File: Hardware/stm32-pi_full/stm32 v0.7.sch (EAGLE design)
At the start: 199 parts, among them Q1 MMBT3906, Q2 MMBT3904, Q3 MMBT3904, U1 ESP32-WROOM-32D

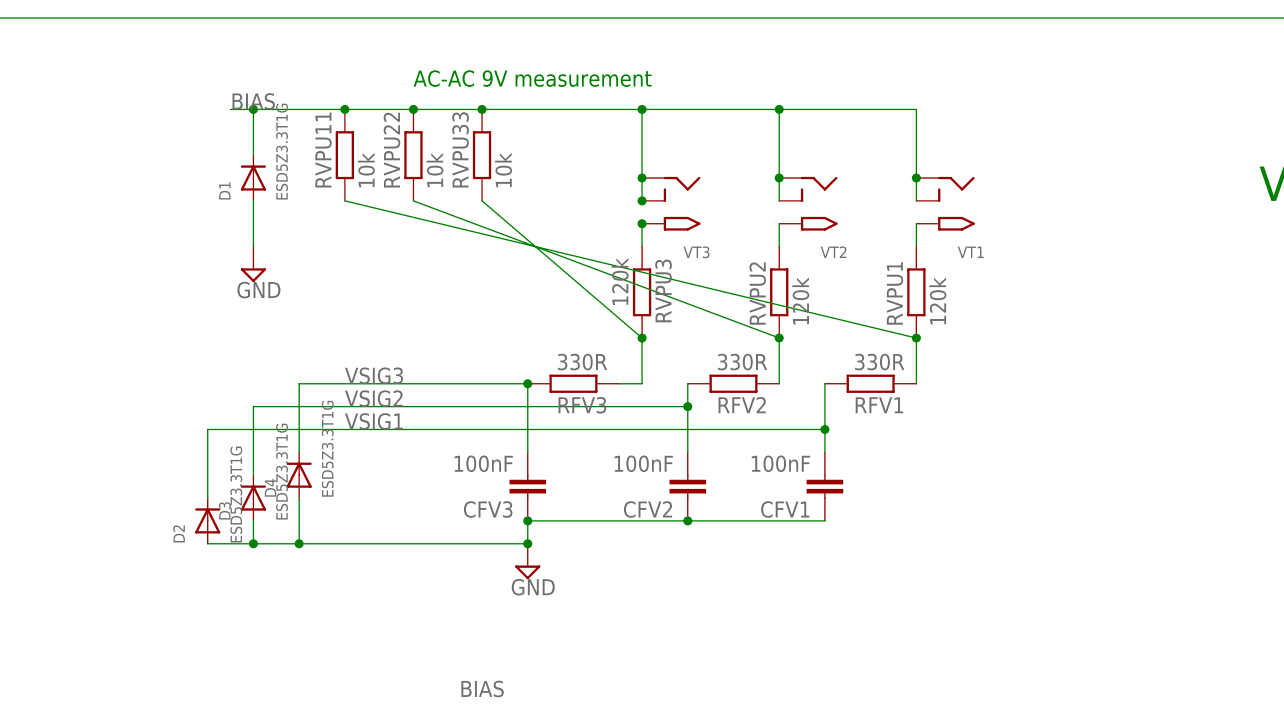
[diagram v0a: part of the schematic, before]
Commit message: commit JSON parser and arm_math examples
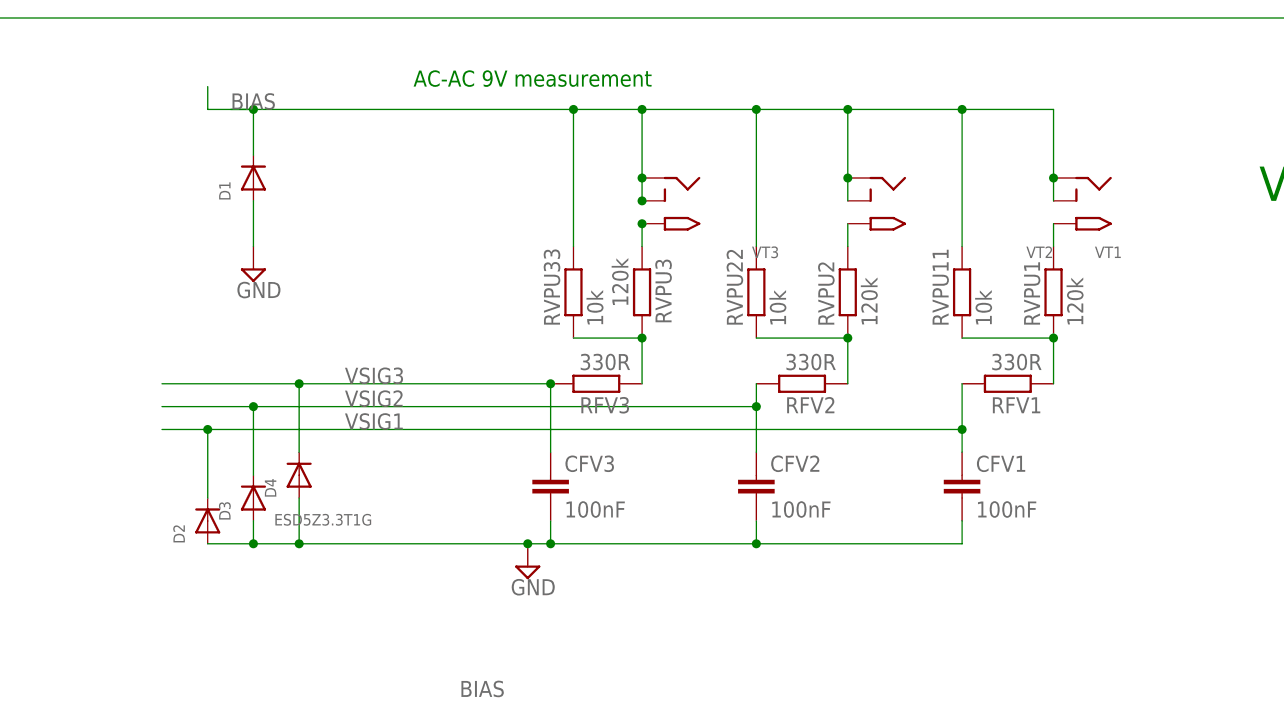
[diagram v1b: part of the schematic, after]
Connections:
- net GND: now also CFV1.2, CFV2.2, CFV3.2; no longer CFV1.1, CFV2.1, CFV3.1
- net VSIG1: now also CFV1.1; no longer CFV1.2
- net VSIG2: now also CFV2.1; no longer CFV2.2
- net VSIG3: now also CFV3.1; no longer CFV3.2
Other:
- moved on the sheet: CFV1, CFV2, CFV3, RFV1, RFV2, RFV3, RVPU1, RVPU11, RVPU2, RVPU22, RVPU33, VT1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

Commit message: update, plus reports
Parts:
- removed 3POLE_1, 3POLE_2, 3POLE_3, 3POLE_6, 3POLE_7: OMNIMATE_LSF_3COMBICON_SMT_3, OMNIMATE_LSF:OMNIMATE_LSF_3COMBICON_SMT_3
- removed C15, C21: 100nF, resistor:C-EUC0603
- removed C23: (no value), rcl:CPOL-EU153CLV-1010
- removed D14, D15, D16, D19: ESD5Z3.3T1G, microbuilder:DIODESOD-523
- removed D20: (no value), diode:SUPPRESSOR-SMBJ
- removed JP3: (no value), pinhead+:PINHD-1X81X08_SMT
- added BIAS_IN, ST_LINK: (no value), SparkFun:M02PTH
- added C1, C19, C20, C22: 100nF, resistor:C-EUC0603
- added D17, D18, D21, D26, D40*1: ESD5Z3.3T1G, microbuilder:DIODESOD-523
- added G1: CH291-1220LF, CH291-1220LF:CH291-1220LF
- added J1, SJ23, SJ24, SJ25, SJ26, SJ27, SJ28, SJ29, SJ30, SJ32: SOLDERJUMPERNO, SparkFun:SOLDERJUMPERNO
- added OLED: (no value), con-lstb-db:MA04-1-OLEDOLED
- added R7: 4.7k, resistor:R-EU_R0603
- added R8: 1k, resistor:R-EU_R0603
- added UART_2: (no value), pinhead+:PINHD-1X61X06_SMT
- C10: value 100nF -> 2.2uF; device resistor:C-EUC0603 -> rcl:C-EUC0805
- C11: value 10nF -> 2.2uF; device rcl:C-EUC0603 -> rcl:C-EUC0805
- C12, C7: value 1uF -> 4.7uF
- C13: value 10nF -> 100nF
- C14, C17: value 1uF -> 2.2uF
- C24, C25, C3, C4: value 4.7uF -> 2.2uF
- C50*: value 1uF -> 2.2uF; device rcl:C-EUC0603 -> rcl:C-EUC0805
- SJ22: value (none) -> SOLDERJUMPERNO; device jumper-con_db:SJ-CONCON -> SparkFun:SOLDERJUMPERNO
- renumbered JP1 to UART_ESP
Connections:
- net N$11 renamed RXD0_ESP
- net N$16 renamed CS_STM32_RPI
- net N$7 renamed TXD0_ESP
- removed net +3V3_ADC: C11.1, C12.1, C7.1, SJ2.2, STM32F303VE.VREF+, VREF_3V3.OUT
- removed net N$21: R6.1, SJ22.2
- removed net N$23: STM32F303VE.PA10, UART1.1
- new net +3V3_ESP: SJ23.1, U1.3V3
- new net BOOT0_RPI: J1.2, PCB2.GPIO4
- new net N$16: Q4.S, R8.1
- new net NRST_STM_ESP: SJ25.1, U1.IO18
- new net NRST_STM_RPI: PCB2.GPIO17, SJ32.2
- new net RPI_GPIO16_RPI: PCB2.GPIO16, SJ29.1
- new net RPI_GPIO20_RPI: PCB2.GPIO20, SJ30.1
- new net RST_RFM_ESP: SJ24.1, U1.IO17
- new net RST_RFM_RPI: PCB2.GPIO5, SJ28.2
- new net SCL_RPI: PCB2.ID_SC*, SJ27.1
- new net SDA_RPI: PCB2.ID_SD*, SJ26.2
- new net VDD_MCP1501: C11.1, SJ22.2, VREF_3V3.SHT_DN, VREF_3V3.VDD
- new net VREF+: SJ2.2, STM32F303VE.VREF+, VREF_3V3.OUT
- net +3V3: now also BIAS_IN.1, OLED.3, R6.1, R7.2, SJ23.2, U$1.P$1, U$3.P$1, U$4.P$1, U$5.P$1; no longer 3POLE_1.1, 3POLE_2.1, 3POLE_3.1, 3POLE_6.1, R22.2, SJ22.1, U1.3V3, UART_ESP.2, VREF_3V3.SHT_DN
- net +5V: now also C10.1, C12.2, C7.1, D40*1.C, SJ22.1, UART_2.3; no longer D20.C, JP3.3, VREF_3V3.VDD
- net 24V: now also U$6.P$1; no longer 3POLE_7.3
- net BOOT0: now also J1.1
- net BUTTON1: now also PCB2.GPIO27; no longer PCB2.GPIO4
- net DS18B20_2_RJ45: now also R7.1, STM32F303VE.PD0
- net GND: now also C1.2, C12.1, C19.2, C20.2, C22.2, D17.A, D18.A, D21.A, D26.A, D40*1.A, G1.-, OLED.4, U$1.P$3, U$3.P$3, U$4.P$3, U$5.P$3, U$6.P$3, UART_2.1; no longer 3POLE_1.3, 3POLE_2.3, 3POLE_3.3, 3POLE_6.3, 3POLE_7.1, C12.2, C15.2, C21.2, C23.-, D14.A, D15.A, D16.A, D19.A, D20.A, JP3.1
- net MBUS_INPUT: now also U$6.P$2; no longer 3POLE_7.2
- net N$1: now also UART_2.2; no longer JP3.2
- net N$12: now also BIAS_IN.2, R22.2; no longer STM32F303VE.PA9, UART1.2
- net NRST_STM: now also SJ25.2, SJ32.1, UART_2.6; no longer JP3.6, PCB2.GPIO6, U1.IO18
- net PUSHIN_1: now also C1.1, D17.C, U$1.P$2; no longer 3POLE_1.2, D14.C
- net PUSHIN_2: now also C19.1, D18.C, U$3.P$2; no longer 3POLE_2.2, C10.1, D15.C
- net PUSHIN_3: now also C20.1, D21.C, U$4.P$2; no longer 3POLE_3.2, C15.1, D16.C
- net PUSHIN_BYANT: now also C22.1, D26.C, U$5.P$2; no longer 3POLE_6.2, C21.1, D19.C
- net RPI_GPIO16: now also SJ29.2; no longer PCB2.GPIO16
- net RPI_GPIO20: now also SJ30.2; no longer PCB2.GPIO20
- net RST_RFM: now also SJ24.2, SJ28.1; no longer PCB2.GPIO5, U1.IO17
- net SCL: now also OLED.2, SJ27.2; no longer PCB2.ID_SC*
- net SDA: now also OLED.1, SJ26.1; no longer PCB2.ID_SD*
- net SWCLK: now also ST_LINK.1; no longer JP3.7
- net SWDIO: now also ST_LINK.2; no longer JP3.8
- net UART1_RX: now also STM32F303VE.PA10, UART1.1
- net UART1_TX: now also STM32F303VE.PA9, UART1.2
- net UART2_RX: now also UART_2.4; no longer JP3.4
- net UART2_TX: now also UART_2.5; no longer JP3.5
- net VBAT: now also G1.+, R8.2; no longer C23.+, Q4.S
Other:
- note added: "BATTERY_BACKUP"
- note added: "BIAS"
- note added: "Connectors"
- note added: "Expansion"
- note added: "LEDs"
- note added: "OLED"
- note added: "PUSH_BUTTON"
- note added: "USB"
- note added: "VTs and CTs"
- note removed: "Combined UART & ST-LINK Standard UART pin order SWDIO + SWCLK added to the top"
- note removed: "VT and CT inputs"
- moved on the sheet: BOOT_STM, C10, C11, C12, C18, C27, C28, C40, C41, C42, C45, C46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

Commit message: board v0.7
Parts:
- removed D24, D25, D40*, D41*: ESD5Z3.3T1G, microbuilder:DIODESOD-523
- removed SJ22: SOLDERJUMPERNO, SparkFun:SOLDERJUMPERNO
- removed UART_2, UART_ESP: (no value), pinhead+:PINHD-1X61X06_SMT
- added C15, C21, C31, C32: 2.2uF, rcl:C-EUC0805
- added C23: 200pF*, rcl:C-EUC0603
- added C29, C30: 5nF, rcl:C-EUC0603
- added JP1: JUMPER-SMT_3_1-NC_TRACE_NO-SILK, SparkFun-Jumpers:JUMPER-SMT_3_1-NC_TRACE_NO-SILK
- added R12: 330R, rcl:R-EU_R0603
- added R13, R20: 10k, resistor:R-EU_R0603
- added R21: 200k, resistor:R-EU_R0603
- added SJ31, SJ33: SOLDERJUMPERNO, SparkFun:SOLDERJUMPERNO
- added SV1, SV2: (no value), con-lstb-db:MA06-1
- C12, C18, C27, C7: value 4.7uF -> 2.2uF
- CT1, CT2, CT3, CT4, CT5, CT6, CT7, CT8, CT9: value STEREO_SMD -> SJ-3523-SMT; MPN (none) -> SJ-3523-SMT
- D40*1: value ESD5Z3.3T1G -> ESD5Z5.0T1G
- HSE: value 8MHZ ~15pFmax -> 406C35E08M00000
- PCB2: value RPI3YA -> TSM-120-01-T-DV
- R10, R3, R4, R5: value 220R -> 330R
- R18, R19: value 1K -> 1k
- R6: value 1.5K -> 1k
- R8: value 1k -> 1.5k
- RB1, RB2, RB3, RB4, RB5, RB6, RB7, RB8, RB9: device resistor:R-EU_R0603 -> rcl:R-EU_R1206
- STM32F303VE: value STM32F303XB -> STM32F303VE
- VT1, VT2, VT3: value 2.1MMJACKSMT -> ADC-028-2-T; MPN (none) -> ADC-028-1-T
- renumbered CFV1 to CV1, CFV2 to CV2, CFV3 to CV3, RFV1 to RV1, RFV2 to RV2, RFV3 to RV3, RVPU1 to R43, RVPU11 to R53, RVPU2 to R42, RVPU22 to R52, RVPU3 to R41, RVPU33 to R51
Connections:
- net MBUS_INPUT renamed MBUS_I/O
- net N$20 renamed ANT
- removed net N$18: D24.A, D25.C
- removed net N$19: D40*.A, D41*.C
- removed net VDD_MCP1501: C11.1, SJ22.2, VREF_3V3.SHT_DN, VREF_3V3.VDD
- removed net VT1_EX: EXPANSION.11
- removed net VT2_EX: EXPANSION.12
- removed net VT3_EX: EXPANSION.13
- new net HSE_OUT_: C29.1, HSE.2, R21.2
- new net MBUS_RX_RPI: PCB2.GPIO23, SJ33.1
- new net MBUS_TX_RPI: PCB2.GPIO18, SJ31.1
- new net N$7: R12.1, R6.2
- net +3V3: now also JP1.1, R13.1, R20.1, U$1.P$3, U$3.P$3, U$4.P$3, U$5.P$3; no longer U$1.P$1, U$3.P$1, U$4.P$1, U$5.P$1
- net +5V: now also C11.1, C15.2, C21.1, C3.1, EXPANSION.26, SV1.3, SV2.3, VREF_3V3.SHT_DN, VREF_3V3.VDD; no longer C3.2, D24.C, D40*.C, EXPANSION.2, SJ22.1, UART_2.3, UART_ESP.3
- net 24V: now also U$6.P$3; no longer U$6.P$1
- net BIAS: no longer CT1.4, CT2.4, CT3.4, CT4.4, CT5.4, CT6.4, CT7.4, CT8.4, CT9.4
- net D+: now also R12.2; no longer R6.2
- net GND: now also C15.1, C21.2, C23.2, C29.2, C3.2, C30.2, C31.2, C32.2, EXPANSION.2, EXPANSION.25, SV1.1, SV2.1, U$1.P$1, U$3.P$1, U$4.P$1, U$5.P$1, U$6.P$1; no longer C3.1, D25.A, D41*.A, EXPANSION.26, U$1.P$3, U$3.P$3, U$4.P$3, U$5.P$3, U$6.P$3, UART_2.1, UART_ESP.1
- net HSE_IN: now also C30.1
- net HSE_OUT: now also R21.1; no longer HSE.2
- net IO8_EX: no longer EXPANSION.25
- net MBUS_RX: now also SJ33.2; no longer PCB2.GPIO23
- net MBUS_TX: now also SJ31.2; no longer PCB2.GPIO18
- net N$1: now also SV1.2; no longer UART_2.2
- net N$12: now also JP1.2
- net N$14: now also SV2.6; no longer UART_ESP.6
- net NRST_STM: now also SV1.6; no longer UART_2.6
- net PC14: now also C31.1
- net PC15: now also C32.1
- net RXD0_ESP: now also SV2.4; no longer UART_ESP.4
- net SCL: now also R13.2
- net SDA: now also R20.2
- net TXD0_ESP: now also SV2.5; no longer UART_ESP.5
- net UART2_RX: now also SV1.4; no longer UART_2.4
- net UART2_TX: now also SV1.5; no longer UART_2.5
- net VREF+: now also C23.1, JP1.3
- net VSIG4: now also EXPANSION.11
- net VSIG5: now also EXPANSION.12
- net VSIG6: now also EXPANSION.13
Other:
- note added: "Frequency 8MHZ to 32MHZ 25pF max."
- note removed: "Frequency 8MHZ to 32MHZ"
- note removed: "Mbus"
- moved on the sheet: C12, C3, D40*1, OLED, R6, ST_LINK, TP4, TP5, TP6, USB-C

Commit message: update dec2019
v0.7 gerbers sent to manf.
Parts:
- removed BIAS_IN: (no value), SparkFun:M02PTH
- removed R12: 330R, rcl:R-EU_R0603
- R6: value 1k -> 1.5k
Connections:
- removed net N$7: R12.1, R6.2
- net +3V3: no longer BIAS_IN.1
- net BIAS: now also CT1.4, CT2.4, CT3.4, CT4.4, CT5.4, CT6.4, CT7.4, CT8.4, CT9.4
- net D+: now also R6.2; no longer R12.2
- net N$12: no longer BIAS_IN.2
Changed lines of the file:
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@@
 <part name="SJ3" library="SparkFun" deviceset="SOLDERJUMPER" device="NO"/>
 <part name="SJ18" library="SparkFun" deviceset="SOLDERJUMPER" device="NO"/>
-<part name="R6" library="rcl" library_urn="urn:adsk.eagle:library:334" deviceset="R-EU_" device="R0603" package3d_urn="urn:adsk.eagle:package:23555/3" value="1k"/>
+<part name="R6" library="rcl" library_urn="urn:adsk.eagle:library:334" deviceset="R-EU_" device="R0603" package3d_urn="urn:adsk.eagle:package:23555/3" value="1.5k"/>
 <part name="SJ19" library="SparkFun" deviceset="SOLDERJUMPER" device="NO"/>
 <part name="SJ20" library="SparkFun" deviceset="SOLDERJUMPER" device="NO"/>
@@
 <part name="+3V3" library="supply1" library_urn="urn:adsk.eagle:library:371" deviceset="+3V3" device=""/>
 <part name="C12" library="rcl" library_urn="urn:adsk.eagle:library:334" deviceset="C-EU" device="C0805" package3d_urn="urn:adsk.eagle:package:23617/2" value="2.2uF"/>
-<part name="BIAS_IN" library="SparkFun" deviceset="M02" device="PTH"/>
 <part name="SJ32" library="SparkFun" deviceset="SOLDERJUMPER" device="NO"/>
 <part name="J1" library="SparkFun" deviceset="SOLDERJUMPER" device="NO"/>
@@
 <part name="SJ33" library="SparkFun" deviceset="SOLDERJUMPER" device="NO"/>
 <part name="C15" library="rcl" library_urn="urn:adsk.eagle:library:334" deviceset="C-EU" device="C0805" package3d_urn="urn:adsk.eagle:package:23617/2" value="2.2uF"/>
-<part name="R12" library="rcl" library_urn="urn:adsk.eagle:library:334" deviceset="R-EU_" device="R0603" package3d_urn="urn:adsk.eagle:package:23555/3" value="330R"/>
 <part name="SV1" library="con-lstb-db" deviceset="MA06-1" device=""/>
 <part name="SV2" library="con-lstb-db" deviceset="MA06-1" device=""/>
@@
 <attribute name="VALUE" x="-130.048" y="190.373" size="1.778" layer="96" rot="R180"/>
 </instance>
-<instance part="BIAS_IN" gate="G$1" x="185.42" y="70.612" smashed="yes" rot="R180">
-<attribute name="VALUE" x="187.96" y="75.692" size="1.778" layer="96" rot="R180"/>
-<attribute name="NAME" x="190.246" y="64.516" size="1.778" layer="95" rot="R180"/>
-</instance>
 <instance part="SJ32" gate="1" x="-167.64" y="33.02" smashed="yes">
 <attribute name="NAME" x="-166.624" y="34.798" size="1.778" layer="95"/>
@@
 <attribute name="VALUE" x="-122.428" y="190.373" size="1.778" layer="96" rot="R180"/>
 </instance>
-<instance part="R12" gate="G$1" x="53.086" y="-25.4" smashed="yes">
-<attribute name="NAME" x="46.482" y="-23.9014" size="1.778" layer="95"/>
-<attribute name="VALUE" x="46.228" y="-28.702" size="1.778" layer="96"/>
-</instance>
 <instance part="SV1" gate="1" x="-71.12" y="-48.26" smashed="yes">
 <attribute name="VALUE" x="-72.39" y="-60.96" size="1.778" layer="96"/>
@@
 <segment>
 <pinref part="+3V4" gate="G$1" pin="+3V3"/>
-<pinref part="BIAS_IN" gate="G$1" pin="1"/>
 <wire x1="177.8" y1="70.612" x2="177.8" y2="73.66" width="0.1524" layer="91"/>
 <pinref part="JP1" gate="G$1" pin="1"/>
@@
 <pinref part="RB15" gate="G$1" pin="2"/>
 <junction x="312.42" y="73.66"/>
+<pinref part="CT6" gate="G$1" pin="4"/>
+<wire x1="317.5" y1="66.04" x2="320.04" y2="66.04" width="0.1524" layer="91"/>
+<wire x1="320.04" y1="66.04" x2="320.04" y2="73.66" width="0.1524" layer="91"/>
+<wire x1="320.04" y1="73.66" x2="317.5" y2="73.66" width="0.1524" layer="91"/>
+<junction x="317.5" y="73.66"/>
 </segment>
 <segment>
@@
 <pinref part="RB14" gate="G$1" pin="2"/>
 <junction x="312.42" y="111.76"/>
+<pinref part="CT5" gate="G$1" pin="4"/>
+<wire x1="317.5" y1="104.14" x2="320.04" y2="104.14" width="0.1524" layer="91"/>
+<wire x1="320.04" y1="104.14" x2="320.04" y2="111.76" width="0.1524" layer="91"/>
+<wire x1="320.04" y1="111.76" x2="317.5" y2="111.76" width="0.1524" layer="91"/>
+<junction x="317.5" y="111.76"/>
 </segment>
 <segment>
@@
 <pinref part="RB13" gate="G$1" pin="2"/>
 <junction x="312.42" y="149.86"/>
+<pinref part="CT4" gate="G$1" pin="4"/>
+<wire x1="317.5" y1="142.24" x2="320.04" y2="142.24" width="0.1524" layer="91"/>
+<wire x1="320.04" y1="142.24" x2="320.04" y2="149.86" width="0.1524" layer="91"/>
+<wire x1="320.04" y1="149.86" x2="317.5" y2="149.86" width="0.1524" layer="91"/>
+<junction x="317.5" y="149.86"/>
 </segment>
 <segment>
@@
 <wire x1="378.46" y1="162.56" x2="378.46" y2="149.86" width="0.1524" layer="91"/>
 <junction x="374.65" y="162.56"/>
+<pinref part="CT3" gate="G$1" pin="4"/>
+<wire x1="381" y1="142.24" x2="383.54" y2="142.24" width="0.1524" layer="91"/>
+<wire x1="383.54" y1="142.24" x2="383.54" y2="149.86" width="0.1524" layer="91"/>
+<wire x1="383.54" y1="149.86" x2="381" y2="149.86" width="0.1524" layer="91"/>
+<junction x="381" y="149.86"/>
 </segment>
 <segment>
@@
 <wire x1="378.46" y1="124.46" x2="378.46" y2="111.76" width="0.1524" layer="91"/>
 <junction x="374.65" y="124.46"/>
+<pinref part="CT2" gate="G$1" pin="4"/>
+<wire x1="381" y1="104.14" x2="383.54" y2="104.14" width="0.1524" layer="91"/>
+<wire x1="383.54" y1="104.14" x2="383.54" y2="111.76" width="0.1524" layer="91"/>
+<wire x1="383.54" y1="111.76" x2="381" y2="111.76" width="0.1524" layer="91"/>
+<junction x="381" y="111.76"/>
 </segment>
 <segment>
@@
 <junction x="374.65" y="86.36"/>
 <junction x="368.3" y="73.66"/>
+<pinref part="CT1" gate="G$1" pin="4"/>
+<wire x1="381" y1="66.04" x2="383.54" y2="66.04" width="0.1524" layer="91"/>
+<wire x1="383.54" y1="66.04" x2="383.54" y2="73.66" width="0.1524" layer="91"/>
+<wire x1="383.54" y1="73.66" x2="381" y2="73.66" width="0.1524" layer="91"/>
+<junction x="381" y="73.66"/>
 </segment>
 <segment>
@@
 <label x="254" y="78.74" size="1.778" layer="95" rot="R180"/>
 <wire x1="220.98" y1="73.66" x2="243.84" y2="73.66" width="0.1524" layer="91"/>
+<pinref part="CT7" gate="G$1" pin="4"/>
+<wire x1="251.46" y1="66.04" x2="254" y2="66.04" width="0.1524" layer="91"/>
+<wire x1="254" y1="66.04" x2="254" y2="73.66" width="0.1524" layer="91"/>
+<wire x1="254" y1="73.66" x2="251.46" y2="73.66" width="0.1524" layer="91"/>
 </segment>
 <segment>
@@
 <label x="254" y="116.84" size="1.778" layer="95" rot="R180"/>
 <wire x1="220.98" y1="111.76" x2="243.84" y2="111.76" width="0.1524" layer="91"/>
+<pinref part="CT8" gate="G$1" pin="4"/>
+<wire x1="251.46" y1="104.14" x2="254" y2="104.14" width="0.1524" layer="91"/>
+<wire x1="254" y1="104.14" x2="254" y2="111.76" width="0.1524" layer="91"/>
+<wire x1="254" y1="111.76" x2="251.46" y2="111.76" width="0.1524" layer="91"/>
 </segment>
 <segment>
@@
 <label x="254" y="154.94" size="1.778" layer="95" rot="R180"/>
 <wire x1="220.98" y1="149.86" x2="243.84" y2="149.86" width="0.1524" layer="91"/>
+<pinref part="CT9" gate="G$1" pin="4"/>
+<wire x1="251.46" y1="142.24" x2="254" y2="142.24" width="0.1524" layer="91"/>
+<wire x1="254" y1="142.24" x2="254" y2="149.86" width="0.1524" layer="91"/>
+<wire x1="254" y1="149.86" x2="251.46" y2="149.86" width="0.1524" layer="91"/>
+<junction x="251.46" y="149.86"/>
 </segment>
 <segment>
@@
 <pinref part="STM32F303VE" gate="G$1" pin="PA12"/>
 <label x="53.34" y="-25.4" size="1.778" layer="95"/>
-<wire x1="63.5" y1="-25.4" x2="58.166" y2="-25.4" width="0.1524" layer="91"/>
-<pinref part="R12" gate="G$1" pin="2"/>
+<wire x1="45.72" y1="-25.4" x2="63.5" y2="-25.4" width="0.1524" layer="91"/>
+<pinref part="R6" gate="G$1" pin="2"/>
+<wire x1="48.006" y1="-25.4" x2="45.72" y2="-25.4" width="0.1524" layer="91"/>
+<junction x="45.72" y="-25.4"/>
 </segment>
 <segment>
@@
 <segment>
 <pinref part="R22" gate="G$1" pin="2"/>
-<pinref part="BIAS_IN" gate="G$1" pin="2"/>
 <wire x1="177.8" y1="63.5" x2="177.8" y2="68.072" width="0.1524" layer="91"/>
 <pinref part="JP1" gate="G$1" pin="2"/>
-<junction x="177.8" y="68.072"/>
 </segment>
 </net>
@@
 </segment>
 </net>
-<net name="N$7" class="0">
-<segment>
-<pinref part="R6" gate="G$1" pin="2"/>
-<wire x1="48.006" y1="-25.4" x2="45.72" y2="-25.4" width="0.1524" layer="91"/>
-<pinref part="R12" gate="G$1" pin="1"/>
-</segment>
-</net>
